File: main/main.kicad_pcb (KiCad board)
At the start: 2 copper layers, 60 x 60 mm, 21 parts, among them J1 conn_I2c_mod, J2 conn_I2c_mod, J3 conn_I2c_mod, J4 conn_spi_mod, J5 conn_spi_mod, J6 conn_spi_mod, J7 Screw_Terminal_01x02, SW1 SW_SPST, U1 ESP32-DEVKITC-32D, U2 SiP32431DR3

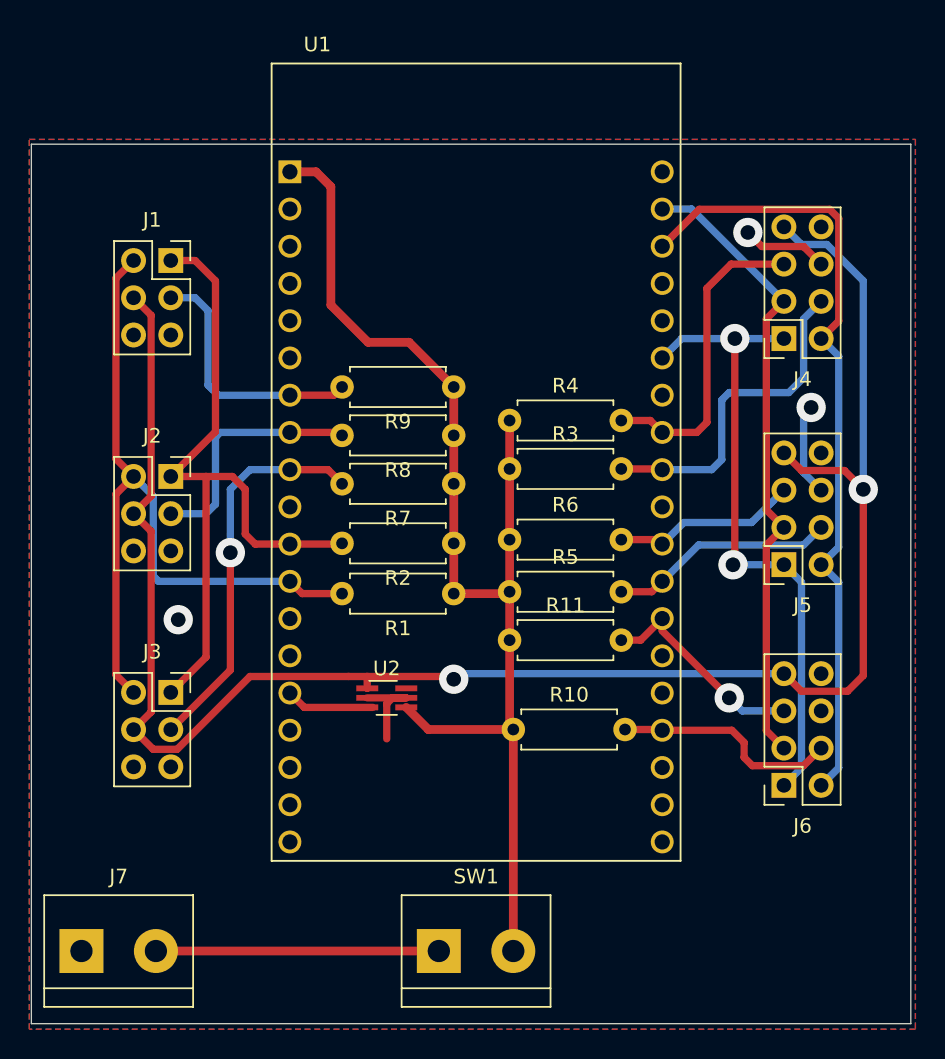
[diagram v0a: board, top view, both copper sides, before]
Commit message: Follow impression restrictions
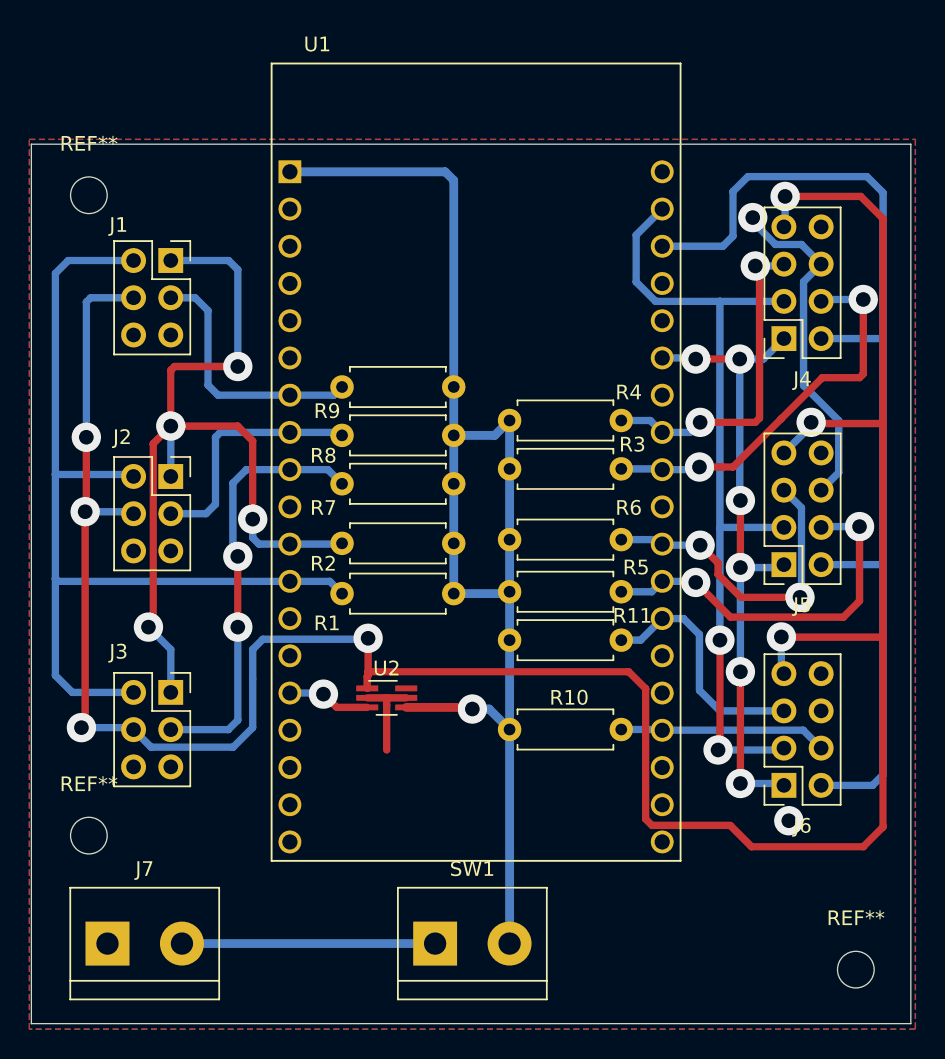
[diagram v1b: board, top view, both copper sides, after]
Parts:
- added REF**: MountingHole_2.5mm, MountingHole:MountingHole_2.5mm, F.Cu at (153.9, 90.2)
- added REF**: MountingHole_2.5mm, MountingHole:MountingHole_2.5mm, F.Cu at (206.2, 99.3)
- added REF**: MountingHole_2.5mm, MountingHole:MountingHole_2.5mm, F.Cu at (153.9, 46.5)
- moved J7 1.85 mm to (155.2, 97.5)
- moved SW1 0.57 mm to (177.5, 97.5)
- moved R10 0.25 mm to (182.6, 82.9)
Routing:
- net /Mod3v3: track 126.1 -> 179.7 mm, vias 2 -> 7
- net /MISO: track 54.5 -> 72.0 mm
- net /SCL: track 49.1 -> 61.7 mm, vias 0 -> 4
- net /MOSI: track 43.4 -> 55.9 mm, vias 0 -> 2
- net /SDA: track 52.2 -> 64.3 mm
- net GND: track 18.8 -> 29.8 mm, vias 3 -> 2
- net /CS2: track 15.5 -> 25.7 mm, vias 0 -> 2
- net /IntrSPI2: track 12.7 -> 22.1 mm, vias 0 -> 2
- net +3V3: track 84.3 -> 92.0 mm, vias 0 -> 1
- net /CS1: track 23.1 -> 27.2 mm, vias 0 -> 2
- net /IntrI2C3: track 26.7 -> 29.4 mm, vias 1 -> 2
- net /PWR_BAT: track 19.3 -> 17.3 mm
- net /IntrSPI3: track 14.8 -> 16.5 mm, vias 1 -> 0
- net /CS3: track 15.5 -> 14.2 mm
- net /IntrSPI1: track 21.5 -> 22.7 mm, vias 0 -> 2
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
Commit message: Improved design with 3v3 zone and GND connections
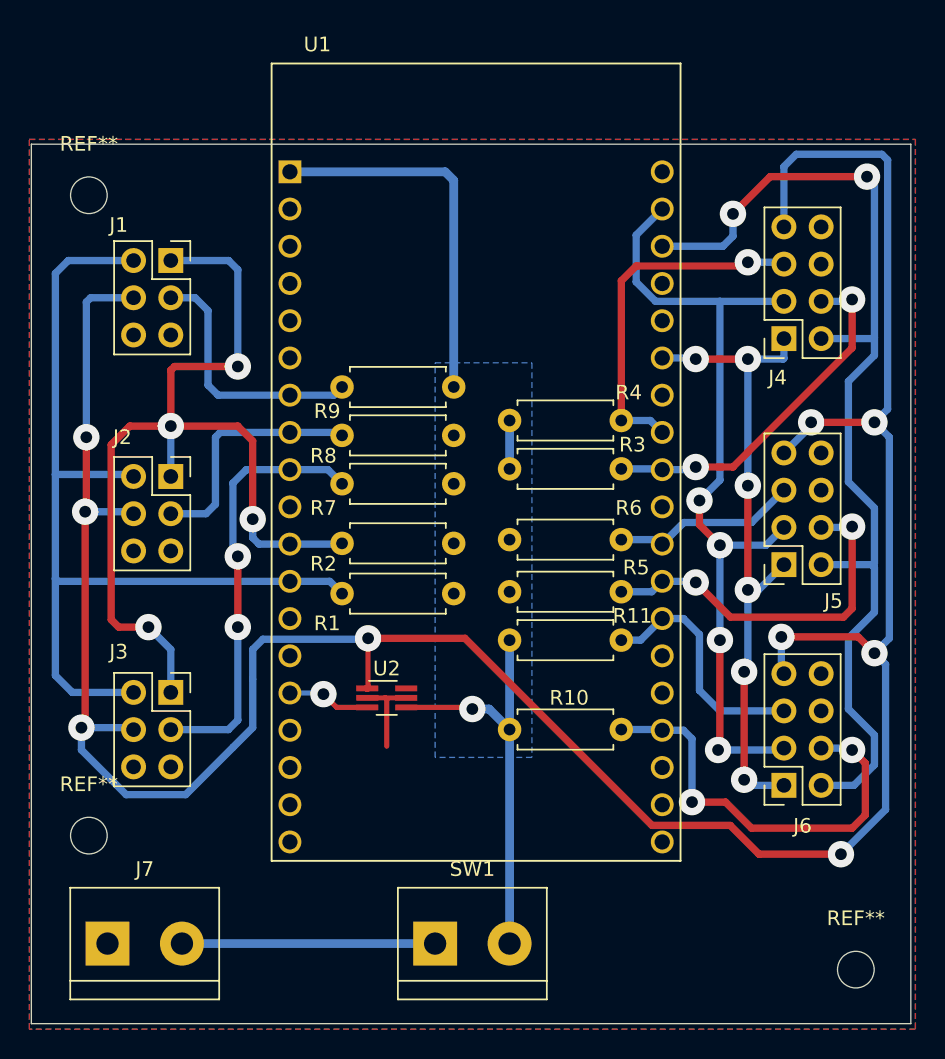
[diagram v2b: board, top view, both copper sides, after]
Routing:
- net +3V3: track 92.0 -> 58.1 mm
- net GND: track 29.8 -> 5.84 mm, vias 2 -> 0
- net /CS3: track 14.2 -> 29.3 mm, vias 0 -> 2
- net /Mod3v3: track 179.7 -> 189.6 mm, vias 7 -> 9
- net /IntrSPI2: track 22.1 -> 12.7 mm, vias 2 -> 0
- net /SCL: track 61.7 -> 66.6 mm
- net /CS1: track 27.2 -> 24.7 mm
- net /IntrSPI1: track 22.7 -> 24.3 mm, vias 2 -> 1
- net /MOSI: track 55.9 -> 57.6 mm, vias 2 -> 4
- net /CS2: track 25.7 -> 25.0 mm
- net /SCK: track 44.0 -> 44.6 mm
- net /MISO: track 72.0 -> 71.5 mm, vias 0 -> 2
- added copper zone on B.Cu, net +3V3
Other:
- net class +3v3: via_dia 2 -> 1.8; via_drill 1 -> 0.8
- net class Default: via_dia 2 -> 1.8; via_drill 1 -> 0.8
- rule via_min_drill: 1 -> 0.8

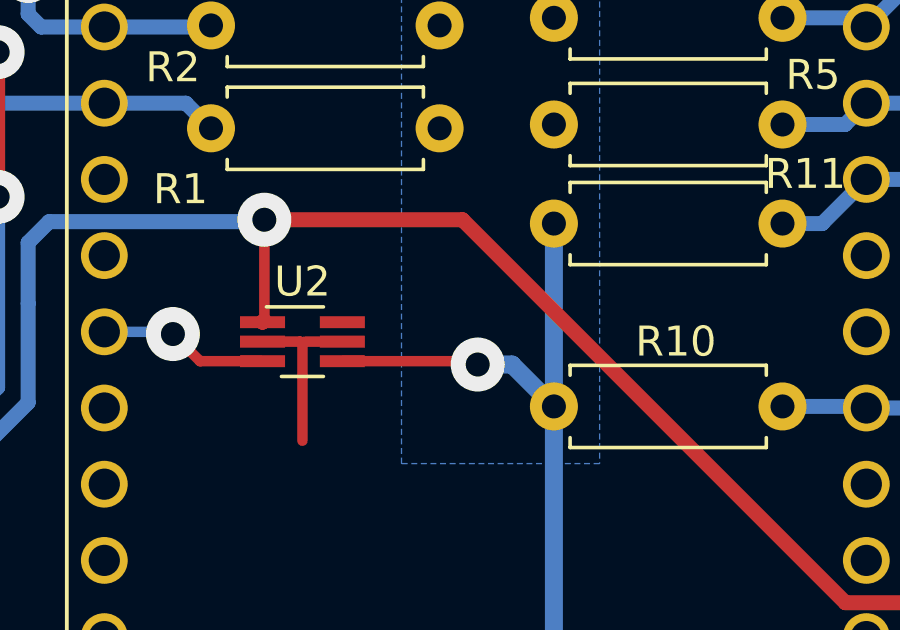
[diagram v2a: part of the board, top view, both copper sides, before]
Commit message: Removed unnecessary 3v3 connections
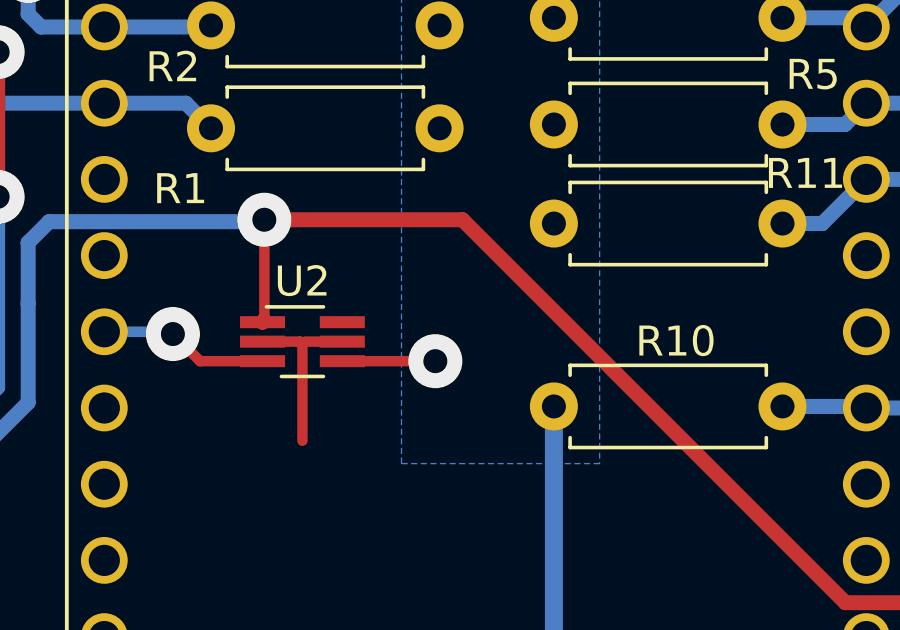
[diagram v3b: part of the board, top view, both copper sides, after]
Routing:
- net +3V3: track 58.1 -> 47.4 mm
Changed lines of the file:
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@@
     (thickness 1.6)
     (drawings 6)
-    (tracks 275)
+    (tracks 271)
     (zones 0)
     (modules 24)
@@
   (segment (start 182.626 61.849) (end 182.626 65.151) (width 0.6) (layer B.Cu) (net 22))
   (segment (start 182.499 83.312) (end 182.88 82.931) (width 0.6) (layer B.Cu) (net 22))
-  (segment (start 182.626 76.835) (end 182.626 82.931) (width 0.6) (layer B.Cu) (net 22))
-  (via (at 180.086 81.534) (size 1.8) (drill 0.8) (layers F.Cu B.Cu) (net 22))
-  (segment (start 179.974 81.422) (end 180.086 81.534) (width 0.6) (layer F.Cu) (net 22))
-  (segment (start 175.574 81.422) (end 179.974 81.422) (width 0.35) (layer F.Cu) (net 22) (status 40000))
-  (segment (start 181.229 81.534) (end 182.626 82.931) (width 0.6) (layer B.Cu) (net 22))
-  (segment (start 180.086 81.534) (end 181.229 81.534) (width 0.6) (layer B.Cu) (net 22))
+  (segment (start 175.574 81.422) (end 178.674 81.422) (width 0.35) (layer F.Cu) (net 22) (status 40000))
   (segment (start 182.626 82.931) (end 182.626 97.536) (width 0.6) (layer B.Cu) (net 22))
+  (via (at 178.674 81.422) (size 1.8) (drill 0.8) (layers F.Cu B.Cu) (net 22))
   (segment (start 170.232 65.203) (end 171.196 66.167) (width 0.5) (layer B.Cu) (net 23))
   (segment (start 167.64 65.203) (end 170.232 65.203) (width 0.5) (layer B.Cu) (net 23))

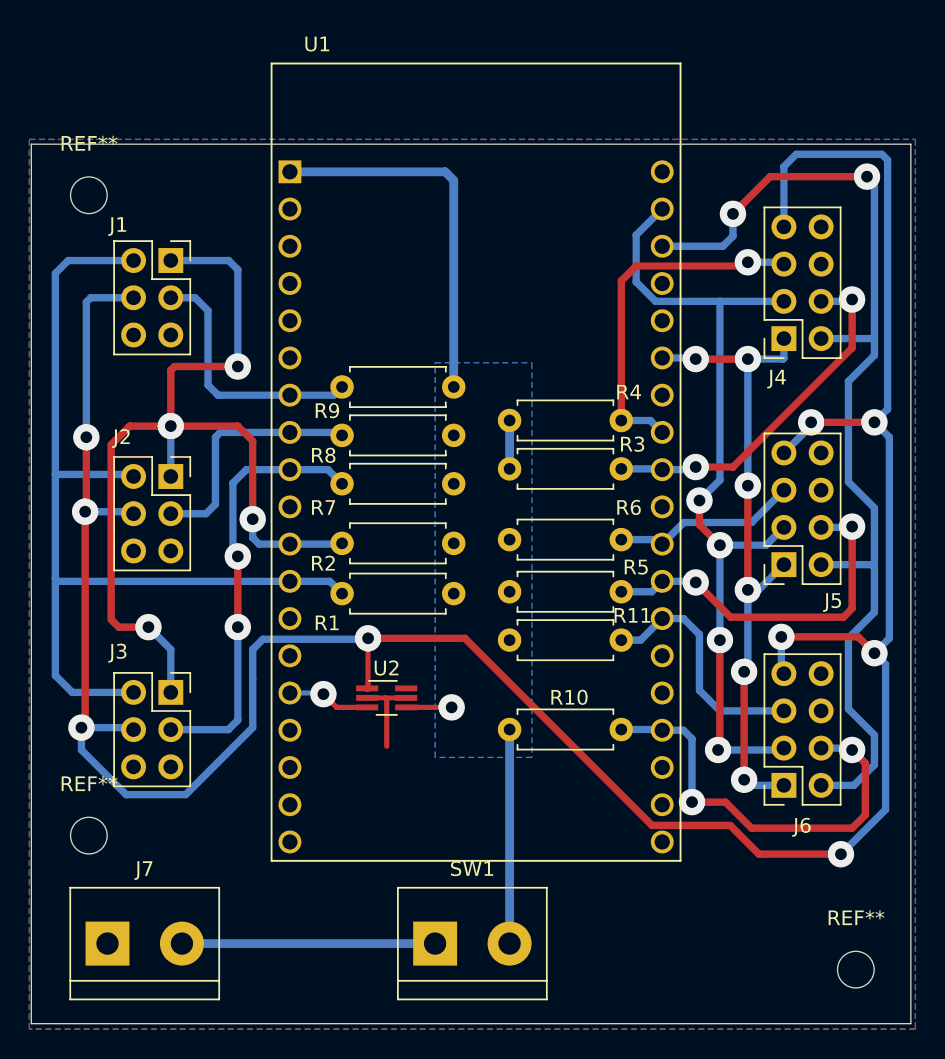
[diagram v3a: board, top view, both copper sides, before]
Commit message: Arreglat farciment massa
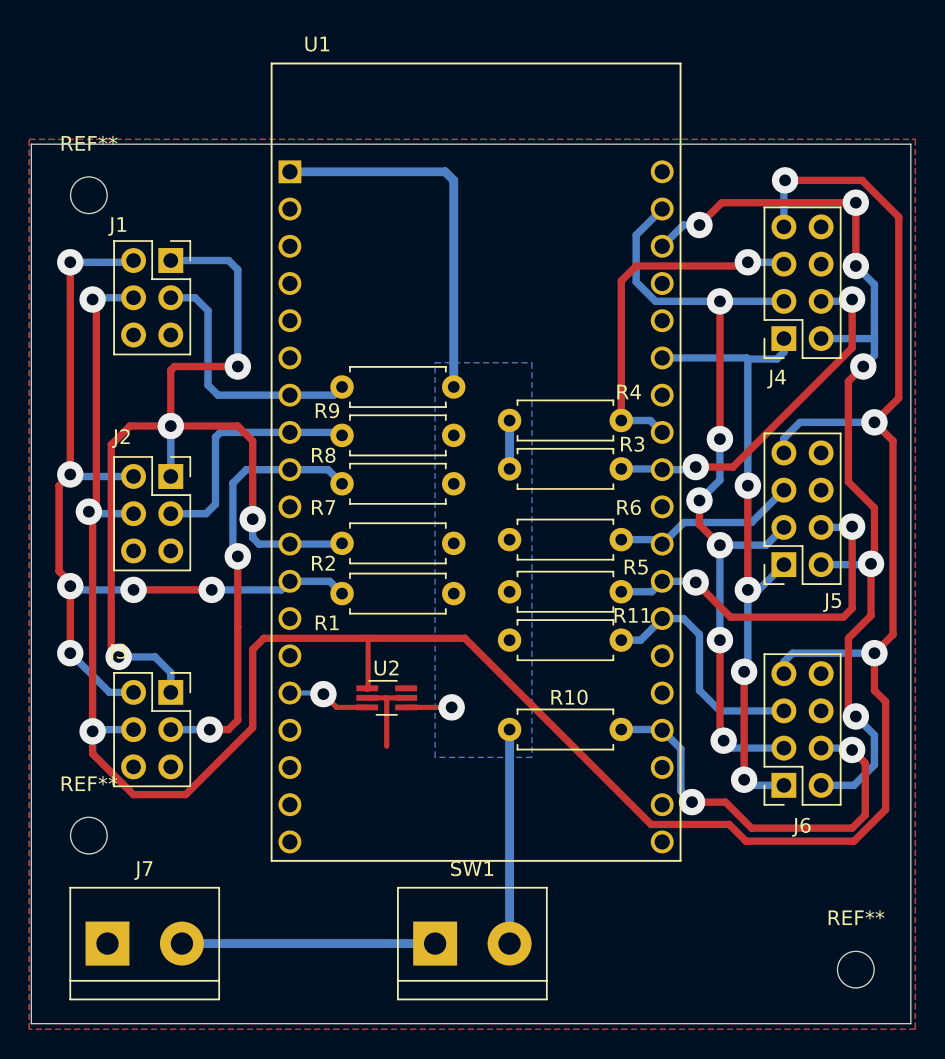
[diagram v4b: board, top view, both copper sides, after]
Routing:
- net /Mod3v3: track 189.6 -> 182.7 mm, vias 9 -> 6
- net /SDA: track 64.3 -> 60.7 mm, vias 0 -> 6
- net /MISO: track 71.5 -> 68.6 mm, vias 2 -> 6
- net /CS3: track 29.3 -> 28.5 mm
- net /MOSI: track 57.6 -> 56.8 mm, vias 4 -> 6
- net /SCK: track 44.6 -> 44.3 mm, vias 6 -> 4
